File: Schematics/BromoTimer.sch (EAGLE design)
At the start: 27 parts, among them IC1 PIC16F687, IC2 7805TV, K1 351, K2 351, Q1 2N3565, Q2 2N3565, Q3 2N3565, X4 22-23-2031, X5 BUZZER

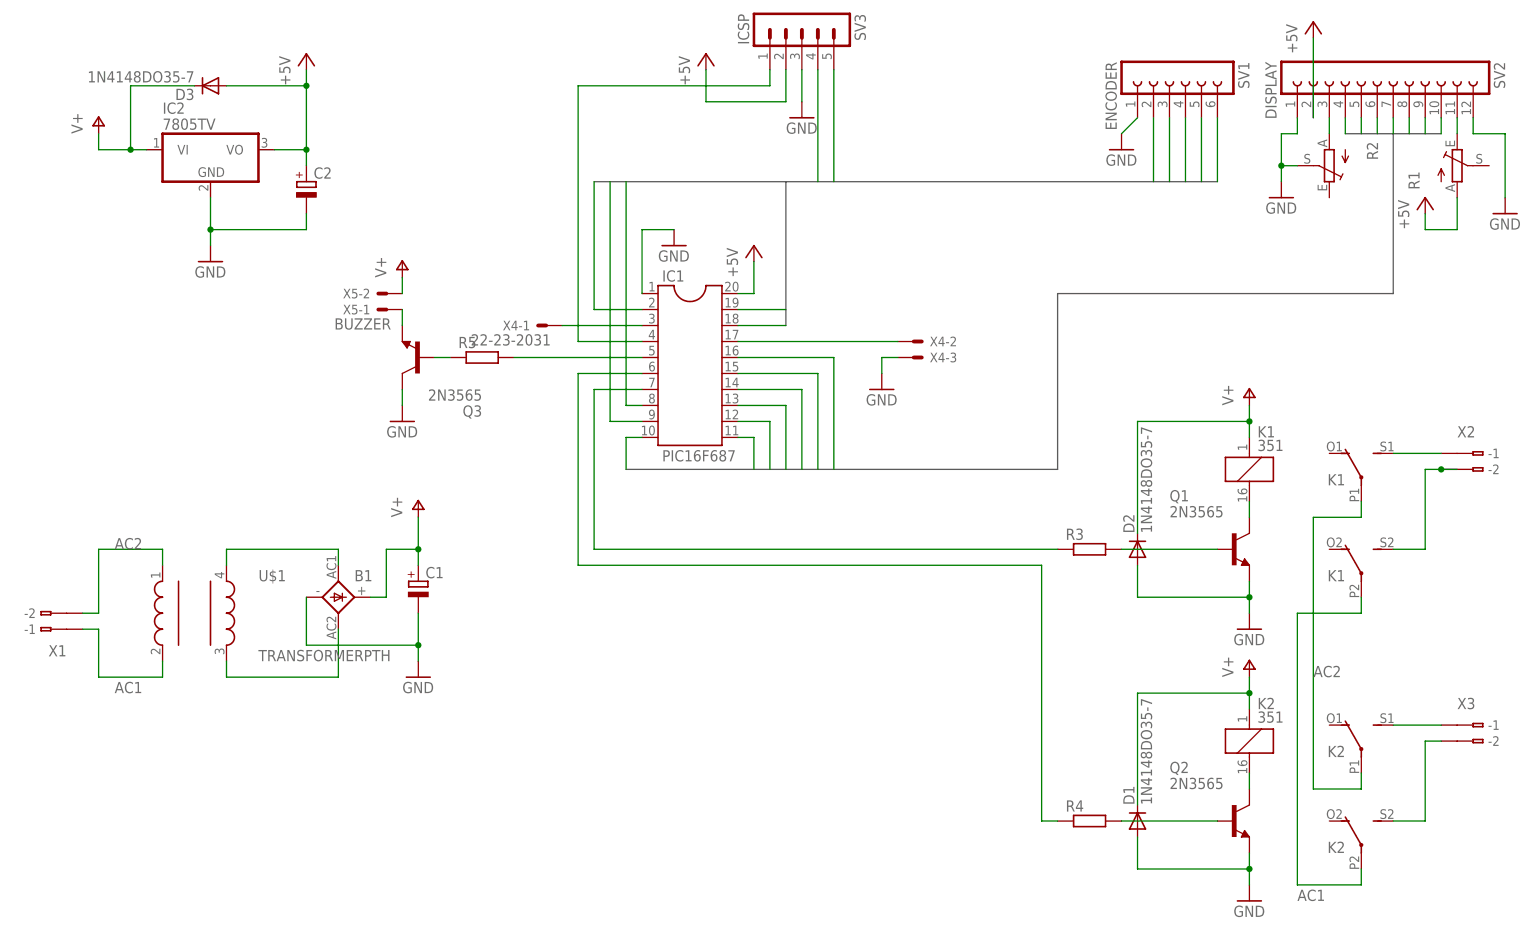
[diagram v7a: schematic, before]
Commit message: Fix bug in relay protection
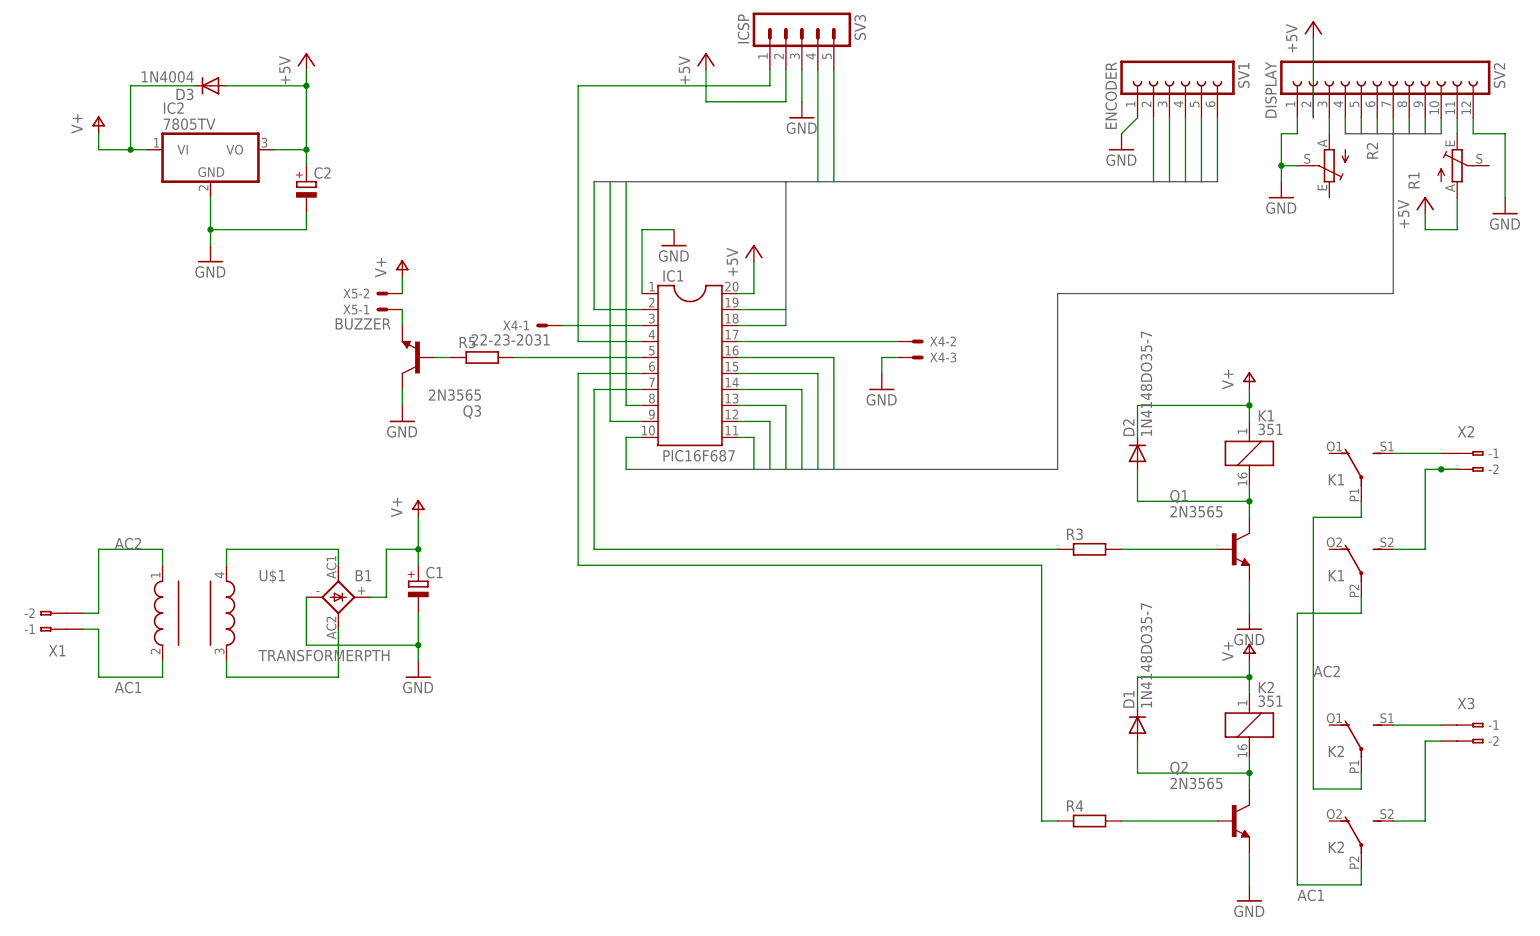
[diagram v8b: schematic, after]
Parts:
- D3: value 1N4148DO35-7 -> 1N4004; device diode:1N4148DO35-7 -> diode:1N4004
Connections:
- net GND: no longer D1.A, D2.A
- net N$6: now also D1.A
- net N$7: now also D2.A
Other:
- moved on the sheet: D1, D2, K1, K2
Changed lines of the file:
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@@
 <part name="P+9" library="supply1" deviceset="+5V" device=""/>
 <part name="GND10" library="supply1" deviceset="GND" device=""/>
-<part name="D3" library="diode" deviceset="1N4148" device="DO35-7"/>
+<part name="D3" library="diode" deviceset="1N4004" device=""/>
 <part name="Q3" library="transistor-npn" deviceset="2N3565" device=""/>
 <part name="R5" library="rcl" deviceset="R-EU_" device="0207/10"/>
@@
 <instance part="X3" gate="G$1" x="243.84" y="58.42"/>
 <instance part="X1" gate="G$1" x="12.7" y="73.66" rot="R180"/>
-<instance part="K1" gate="1" x="205.74" y="99.06"/>
+<instance part="K1" gate="1" x="205.74" y="101.6"/>
 <instance part="K1" gate="2" x="223.52" y="96.52" rot="MR0"/>
 <instance part="K1" gate="3" x="223.52" y="81.28" rot="MR0"/>
-<instance part="K2" gate="1" x="205.74" y="55.88"/>
+<instance part="K2" gate="1" x="205.74" y="58.42"/>
 <instance part="K2" gate="2" x="223.52" y="53.34" rot="MR0"/>
 <instance part="K2" gate="3" x="223.52" y="38.1" rot="MR0"/>
@@
 <instance part="P+8" gate="1" x="22.86" y="154.94"/>
 <instance part="GND8" gate="1" x="185.42" y="149.86"/>
-<instance part="P+5" gate="1" x="205.74" y="68.58"/>
-<instance part="P+6" gate="1" x="205.74" y="111.76"/>
-<instance part="D1" gate="G$1" x="187.96" y="43.18" rot="R90"/>
-<instance part="D2" gate="G$1" x="187.96" y="86.36" rot="R90"/>
+<instance part="P+5" gate="1" x="205.74" y="71.12"/>
+<instance part="P+6" gate="1" x="205.74" y="114.3"/>
+<instance part="D1" gate="G$1" x="187.96" y="58.42" rot="R90"/>
+<instance part="D2" gate="G$1" x="187.96" y="101.6" rot="R90"/>
 <instance part="SV3" gate="G$1" x="134.62" y="170.18" rot="R270"/>
 <instance part="P+9" gate="1" x="119.38" y="165.1"/>
 <instance part="GND10" gate="1" x="134.62" y="154.94"/>
-<instance part="D3" gate="G$1" x="40.64" y="160.02" rot="R180"/>
+<instance part="D3" gate="1" x="40.64" y="160.02" rot="R180"/>
 <instance part="Q3" gate="G$1" x="73.66" y="116.84" rot="R180"/>
 <instance part="R5" gate="G$1" x="83.82" y="116.84"/>
@@
 <pinref part="C2" gate="G$1" pin="+"/>
 <wire x1="55.88" y1="147.32" x2="55.88" y2="149.86" width="0.1524" layer="91"/>
-<pinref part="D3" gate="G$1" pin="A"/>
+<pinref part="D3" gate="1" pin="A"/>
 <wire x1="43.18" y1="160.02" x2="55.88" y2="160.02" width="0.1524" layer="91"/>
 <wire x1="55.88" y1="160.02" x2="55.88" y2="149.86" width="0.1524" layer="91"/>
@@
 <pinref part="Q1" gate="G$1" pin="E"/>
 <pinref part="GND5" gate="1" pin="GND"/>
-<wire x1="205.74" y1="81.28" x2="205.74" y2="78.74" width="0.1524" layer="91"/>
-<pinref part="D2" gate="G$1" pin="A"/>
-<wire x1="205.74" y1="78.74" x2="205.74" y2="76.2" width="0.1524" layer="91"/>
-<wire x1="187.96" y1="83.82" x2="187.96" y2="78.74" width="0.1524" layer="91"/>
-<wire x1="187.96" y1="78.74" x2="205.74" y2="78.74" width="0.1524" layer="91"/>
-<junction x="205.74" y="78.74"/>
+<wire x1="205.74" y1="81.28" x2="205.74" y2="76.2" width="0.1524" layer="91"/>
 </segment>
 <segment>
 <pinref part="Q2" gate="G$1" pin="E"/>
 <pinref part="GND6" gate="1" pin="GND"/>
-<wire x1="205.74" y1="38.1" x2="205.74" y2="35.56" width="0.1524" layer="91"/>
-<pinref part="D1" gate="G$1" pin="A"/>
-<wire x1="205.74" y1="35.56" x2="205.74" y2="33.02" width="0.1524" layer="91"/>
-<wire x1="187.96" y1="40.64" x2="187.96" y2="35.56" width="0.1524" layer="91"/>
-<wire x1="187.96" y1="35.56" x2="205.74" y2="35.56" width="0.1524" layer="91"/>
-<junction x="205.74" y="35.56"/>
+<wire x1="205.74" y1="38.1" x2="205.74" y2="33.02" width="0.1524" layer="91"/>
 </segment>
 <segment>
@@
 <wire x1="205.74" y1="48.26" x2="205.74" y2="50.8" width="0.1524" layer="91"/>
 <pinref part="K2" gate="1" pin="2"/>
+<pinref part="D1" gate="G$1" pin="A"/>
+<wire x1="205.74" y1="50.8" x2="205.74" y2="53.34" width="0.1524" layer="91"/>
+<wire x1="187.96" y1="55.88" x2="187.96" y2="50.8" width="0.1524" layer="91"/>
+<wire x1="187.96" y1="50.8" x2="205.74" y2="50.8" width="0.1524" layer="91"/>
+<junction x="205.74" y="50.8"/>
 </segment>
 </net>
@@
 <segment>
 <pinref part="Q1" gate="G$1" pin="C"/>
+<wire x1="205.74" y1="96.52" x2="205.74" y2="93.98" width="0.1524" layer="91"/>
+<pinref part="K1" gate="1" pin="2"/>
+<pinref part="D2" gate="G$1" pin="A"/>
 <wire x1="205.74" y1="93.98" x2="205.74" y2="91.44" width="0.1524" layer="91"/>
-<pinref part="K1" gate="1" pin="2"/>
+<wire x1="187.96" y1="99.06" x2="187.96" y2="93.98" width="0.1524" layer="91"/>
+<wire x1="187.96" y1="93.98" x2="205.74" y2="93.98" width="0.1524" layer="91"/>
+<junction x="205.74" y="93.98"/>
 </segment>
 </net>
@@
 <pinref part="IC2" gate="A1" pin="VI"/>
 <wire x1="22.86" y1="149.86" x2="27.94" y2="149.86" width="0.1524" layer="91"/>
-<pinref part="D3" gate="G$1" pin="C"/>
+<pinref part="D3" gate="1" pin="C"/>
 <wire x1="27.94" y1="149.86" x2="30.48" y2="149.86" width="0.1524" layer="91"/>
 <wire x1="38.1" y1="160.02" x2="27.94" y2="160.02" width="0.1524" layer="91"/>
@@
 <segment>
 <pinref part="K2" gate="1" pin="1"/>
-<wire x1="205.74" y1="66.04" x2="205.74" y2="63.5" width="0.1524" layer="91"/>
+<wire x1="205.74" y1="68.58" x2="205.74" y2="66.04" width="0.1524" layer="91"/>
 <pinref part="P+5" gate="1" pin="V+"/>
 <pinref part="D1" gate="G$1" pin="C"/>
-<wire x1="205.74" y1="63.5" x2="205.74" y2="60.96" width="0.1524" layer="91"/>
-<wire x1="187.96" y1="45.72" x2="187.96" y2="63.5" width="0.1524" layer="91"/>
-<wire x1="187.96" y1="63.5" x2="205.74" y2="63.5" width="0.1524" layer="91"/>
-<junction x="205.74" y="63.5"/>
+<wire x1="205.74" y1="66.04" x2="205.74" y2="63.5" width="0.1524" layer="91"/>
+<wire x1="187.96" y1="60.96" x2="187.96" y2="66.04" width="0.1524" layer="91"/>
+<wire x1="187.96" y1="66.04" x2="205.74" y2="66.04" width="0.1524" layer="91"/>
+<junction x="205.74" y="66.04"/>
 </segment>
 <segment>
 <pinref part="K1" gate="1" pin="1"/>
-<wire x1="205.74" y1="109.22" x2="205.74" y2="106.68" width="0.1524" layer="91"/>
+<wire x1="205.74" y1="111.76" x2="205.74" y2="109.22" width="0.1524" layer="91"/>
 <pinref part="P+6" gate="1" pin="V+"/>
 <pinref part="D2" gate="G$1" pin="C"/>
-<wire x1="205.74" y1="106.68" x2="205.74" y2="104.14" width="0.1524" layer="91"/>
-<wire x1="187.96" y1="88.9" x2="187.96" y2="106.68" width="0.1524" layer="91"/>
-<wire x1="187.96" y1="106.68" x2="205.74" y2="106.68" width="0.1524" layer="91"/>
-<junction x="205.74" y="106.68"/>
-</segment>
-<segment>
+<wire x1="205.74" y1="109.22" x2="205.74" y2="106.68" width="0.1524" layer="91"/>
+<wire x1="187.96" y1="104.14" x2="187.96" y2="109.22" width="0.1524" layer="91"/>
+<wire x1="187.96" y1="109.22" x2="205.74" y2="109.22" width="0.1524" layer="91"/>
+<junction x="205.74" y="109.22"/>
+</segment>
+<segment>
